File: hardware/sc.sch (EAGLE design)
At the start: 102 parts, among them K1 RT424F124, K2 RT424F124, Q1 si2305cd, Q2 8MHz, Q3 si2305cd, Q4 si2305cd, Q5 si2305cd, Q7 si2305cd, T1 BC846, T2 BC846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

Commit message: calculate resistor dividers and XT1, XT2 load caps
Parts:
- C13: value 10p -> 10pF
- C14: value 100n -> 100nF
- C18, C19: value 100nF -> 10nF
- C21, C22: value 22p -> 33pF
- C23, C24: value 22p -> 22pF
- C4: value 470pF -> 1uF
- LED2: value green -> orange
- Q2: value 8MHz -> 8MHz 18pF
- R15: value NA -> 56k
- R22, R25: value 100k -> 2M
- R24, R26: value 100k -> 240k
- Y1: value 32768Hz -> 32768Hz CFPX-217 12.5pF
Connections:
- net VBAT_IN renamed PV+
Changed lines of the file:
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@@
 <part name="GND4" library="SparkFun" deviceset="GND" device=""/>
 <part name="GND5" library="SparkFun" deviceset="GND" device=""/>
-<part name="C4" library="rcl" deviceset="C-EU" device="C0805" value="470pF"/>
+<part name="C4" library="rcl" deviceset="C-EU" device="C0805" value="1uF"/>
 <part name="GND6" library="SparkFun" deviceset="GND" device=""/>
 <part name="C6" library="rcl" deviceset="C-EU" device="C0805" value="100nF"/>
@@
 <part name="R7" library="rcl" deviceset="R-EU_" device="R0805W" value="4.7k"/>
 <part name="GND26" library="SparkFun" deviceset="GND" device=""/>
-<part name="Q2" library="Omat_komponentit" deviceset="CRYTAL" device="" value="8MHz"/>
-<part name="C21" library="rcl" deviceset="C-EU" device="C0805" value="22p"/>
-<part name="C22" library="rcl" deviceset="C-EU" device="C0805" value="22p"/>
-<part name="Y1" library="Simplex-FreqCtrl" deviceset="CRYSTAL" device="3.2X1.5" value="32768Hz"/>
-<part name="C23" library="rcl" deviceset="C-EU" device="C0805" value="22p"/>
-<part name="C24" library="rcl" deviceset="C-EU" device="C0805" value="22p"/>
+<part name="Q2" library="Omat_komponentit" deviceset="CRYTAL" device="" value="8MHz 18pF"/>
+<part name="C21" library="rcl" deviceset="C-EU" device="C0805" value="33pF"/>
+<part name="C22" library="rcl" deviceset="C-EU" device="C0805" value="33pF"/>
+<part name="Y1" library="Simplex-FreqCtrl" deviceset="CRYSTAL" device="3.2X1.5" value="32768Hz CFPX-217 12.5pF"/>
+<part name="C23" library="rcl" deviceset="C-EU" device="C0805" value="22pF"/>
+<part name="C24" library="rcl" deviceset="C-EU" device="C0805" value="22pF"/>
 <part name="GND33" library="SparkFun" deviceset="GND" device=""/>
 <part name="GND35" library="SparkFun" deviceset="GND" device=""/>
@@
 <part name="GND49" library="SparkFun" deviceset="GND" device=""/>
 <part name="R21" library="rcl" deviceset="R-EU_" device="R0805W" value="10k"/>
-<part name="R22" library="rcl" deviceset="R-EU_" device="R0805W" value="100k"/>
-<part name="R24" library="rcl" deviceset="R-EU_" device="R0805W" value="100k"/>
-<part name="R25" library="rcl" deviceset="R-EU_" device="R0805W" value="100k"/>
-<part name="R26" library="rcl" deviceset="R-EU_" device="R0805W" value="100k"/>
+<part name="R22" library="rcl" deviceset="R-EU_" device="R0805W" value="2M"/>
+<part name="R24" library="rcl" deviceset="R-EU_" device="R0805W" value="240k"/>
+<part name="R25" library="rcl" deviceset="R-EU_" device="R0805W" value="2M"/>
+<part name="R26" library="rcl" deviceset="R-EU_" device="R0805W" value="240k"/>
 <part name="GND34" library="SparkFun" deviceset="GND" device=""/>
 <part name="JP2" library="SparkFun" deviceset="M02" device="PTH" value="bat"/>
@@
 <part name="+3V2" library="supply1" deviceset="+3V3" device=""/>
 <part name="R13" library="rcl" deviceset="R-EU_" device="R0805W" value="100k"/>
-<part name="R15" library="rcl" deviceset="R-EU_" device="R0805W" value="NA"/>
+<part name="R15" library="rcl" deviceset="R-EU_" device="R0805W" value="56k"/>
 <part name="GND14" library="SparkFun" deviceset="GND" device=""/>
 <part name="C5" library="rcl" deviceset="C-EU" device="C0805" value="100nF"/>
@@
 <part name="GND20" library="SparkFun" deviceset="GND" device=""/>
 <part name="C12" library="rcl" deviceset="C-EU" device="C0805" value="10p"/>
-<part name="C13" library="rcl" deviceset="C-EU" device="C0805" value="10p"/>
+<part name="C13" library="rcl" deviceset="C-EU" device="C0805" value="10pF"/>
 <part name="GND21" library="SparkFun" deviceset="GND" device=""/>
 <part name="U$6" library="SparkFun-Connectors" deviceset="USB-MINIB" device="-5PIN"/>
@@
 <part name="R32" library="rcl" deviceset="R-EU_" device="R0805W" value="100"/>
 <part name="GND28" library="SparkFun" deviceset="GND" device=""/>
-<part name="C14" library="rcl" deviceset="C-EU" device="C0805" value="100n"/>
+<part name="C14" library="rcl" deviceset="C-EU" device="C0805" value="100nF"/>
 <part name="R33" library="rcl" deviceset="R-EU_" device="R0805W" value="33k"/>
 <part name="GND29" library="SparkFun" deviceset="GND" device=""/>
@@
 <part name="GND46" library="SparkFun" deviceset="GND" device=""/>
 <part name="U$8" library="Simplex-Switches" deviceset="TACT_SW" device="" value="USB_BSL"/>
-<part name="C18" library="rcl" deviceset="C-EU" device="C0805" value="100nF"/>
-<part name="C19" library="rcl" deviceset="C-EU" device="C0805" value="100nF"/>
+<part name="C18" library="rcl" deviceset="C-EU" device="C0805" value="10nF"/>
+<part name="C19" library="rcl" deviceset="C-EU" device="C0805" value="10nF"/>
 <part name="JP1" library="SparkFun-Connectors" deviceset="M04" device="PTH" value="i2c"/>
 <part name="SUPPLY1" library="Simplex-Power" deviceset="VCC_EN" device=""/>
@@
 <part name="SUPPLY13" library="Simplex-Power" deviceset="VCC_EN" device=""/>
 <part name="X1" library="con-phoenix-508" deviceset="MKDSN1,5/2-5,08" device=""/>
-<part name="LED2" library="led" deviceset="LED" device="CHIP-LED0805" value="green"/>
+<part name="LED2" library="led" deviceset="LED" device="CHIP-LED0805" value="orange"/>
 <part name="R27" library="rcl" deviceset="R-EU_" device="R0805W" value="1K"/>
 <part name="GND36" library="SparkFun" deviceset="GND" device=""/>
@@
 </segment>
 </net>
-<net name="VBAT_IN" class="0">
+<net name="PV+" class="0">
 <segment>
 <wire x1="71.12" y1="91.44" x2="76.2" y2="91.44" width="0.1524" layer="91"/>

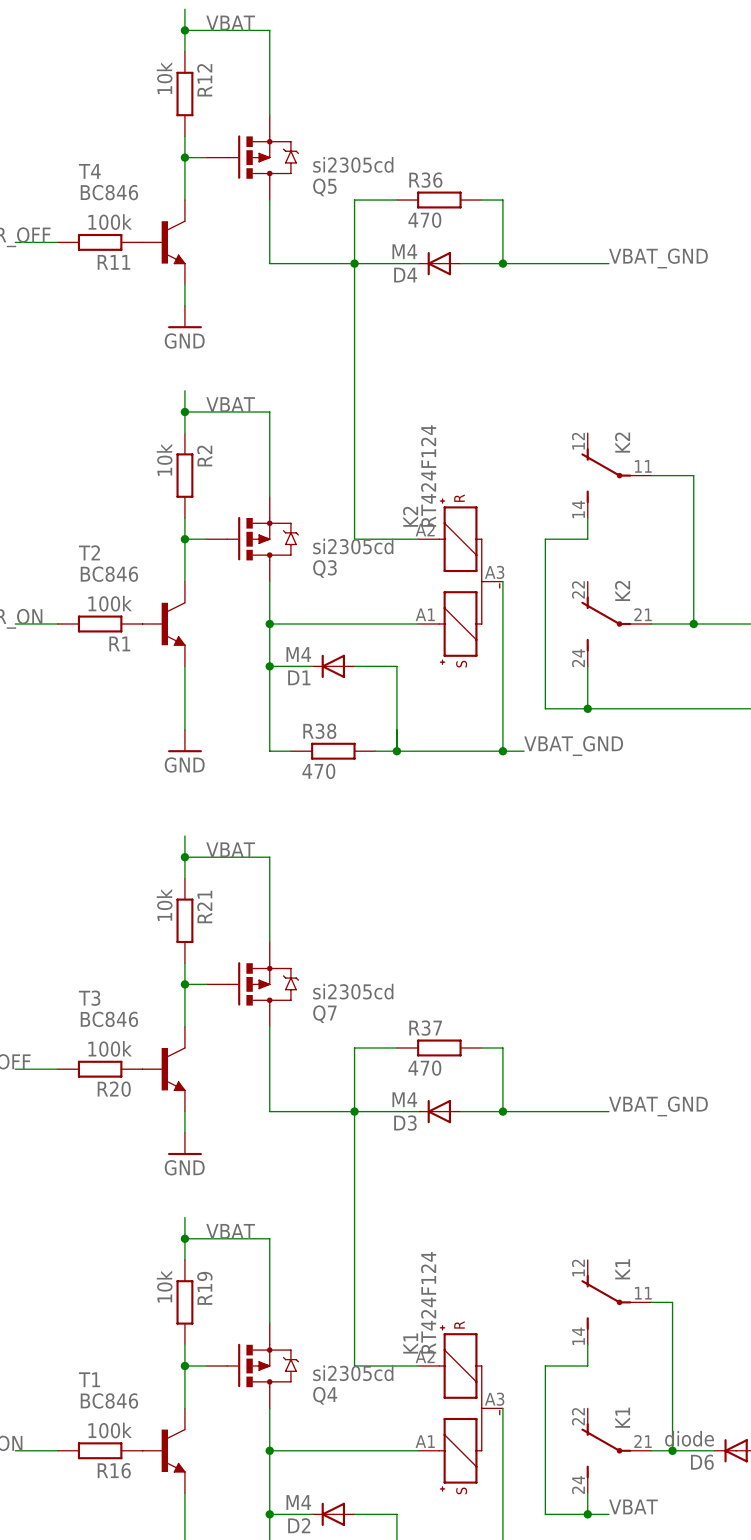
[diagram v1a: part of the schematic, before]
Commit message: use different p-mosfet
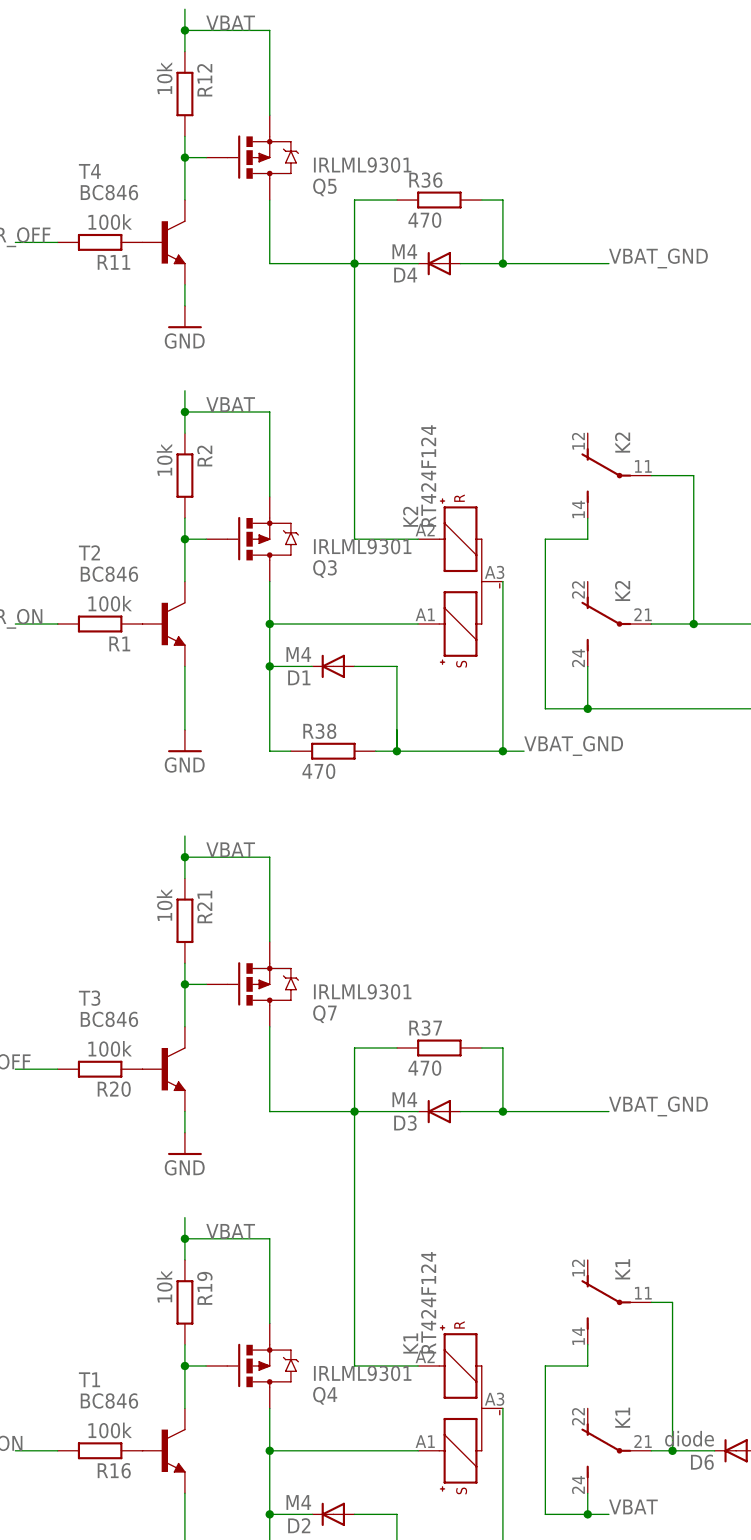
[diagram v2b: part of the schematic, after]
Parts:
- Q3, Q4, Q5, Q7: value si2305cd -> IRLML9301
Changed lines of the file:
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@@
 <part name="GND37" library="SparkFun" deviceset="GND" device=""/>
 <part name="GND47" library="SparkFun" deviceset="GND" device=""/>
-<part name="Q4" library="Simplex-DiscreteSemi" deviceset="MOSFET-PCHANNEL" device="SMD_POWER" value="si2305cd"/>
+<part name="Q4" library="Simplex-DiscreteSemi" deviceset="MOSFET-PCHANNEL" device="SMD_POWER" value="IRLML9301"/>
 <part name="T1" library="transistor" deviceset="BC846" device=""/>
 <part name="R16" library="rcl" deviceset="R-EU_" device="R0805W" value="100k"/>
 <part name="GND48" library="SparkFun" deviceset="GND" device=""/>
 <part name="R19" library="rcl" deviceset="R-EU_" device="R0805W" value="10k"/>
-<part name="Q7" library="Simplex-DiscreteSemi" deviceset="MOSFET-PCHANNEL" device="SMD_POWER" value="si2305cd"/>
+<part name="Q7" library="Simplex-DiscreteSemi" deviceset="MOSFET-PCHANNEL" device="SMD_POWER" value="IRLML9301"/>
 <part name="T3" library="transistor" deviceset="BC846" device=""/>
 <part name="R20" library="rcl" deviceset="R-EU_" device="R0805W" value="100k"/>
@@
 <part name="GND1" library="SparkFun" deviceset="GND" device=""/>
 <part name="K2" library="relay" deviceset="RT424F*" device="4" technology="12"/>
-<part name="Q3" library="Simplex-DiscreteSemi" deviceset="MOSFET-PCHANNEL" device="SMD_POWER" value="si2305cd"/>
+<part name="Q3" library="Simplex-DiscreteSemi" deviceset="MOSFET-PCHANNEL" device="SMD_POWER" value="IRLML9301"/>
 <part name="T2" library="transistor" deviceset="BC846" device=""/>
 <part name="R1" library="rcl" deviceset="R-EU_" device="R0805W" value="100k"/>
 <part name="GND7" library="SparkFun" deviceset="GND" device=""/>
 <part name="R2" library="rcl" deviceset="R-EU_" device="R0805W" value="10k"/>
-<part name="Q5" library="Simplex-DiscreteSemi" deviceset="MOSFET-PCHANNEL" device="SMD_POWER" value="si2305cd"/>
+<part name="Q5" library="Simplex-DiscreteSemi" deviceset="MOSFET-PCHANNEL" device="SMD_POWER" value="IRLML9301"/>
 <part name="T4" library="transistor" deviceset="BC846" device=""/>
 <part name="R11" library="rcl" deviceset="R-EU_" device="R0805W" value="100k"/>

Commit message: rev3
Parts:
- removed D1, D3, D4: M4, SparkFun-DiscreteSemi:DIODESMA
- removed D6: diode, diode:DIODE-C1702-05
- removed K1, K2: RT424F124, relay:RT424F124
- removed Q4, Q5, Q7: IRLML9301, Simplex-DiscreteSemi:MOSFET-PCHANNELSMD_POWER
- removed R1: 100k, rcl:R-EU_R0805W
- removed R37, R38, R39: 470, rcl:R-EU_R0805W
- removed SJ1: pwr_sel, jumper:SJ2W
- removed T2, T3, T4: BC846, transistor:BC846
- removed X1, X4: MKDSN1,5/2-5,08, con-phoenix-508:MKDSN1,5/2-5,08
- added C25, C28: 100nF, rcl:C-EUC0805
- added C26: 1uF, SparkFun-Capacitors:CAP_POLD
- added C27: 10uF, SparkFun-Capacitors:CAP_POLD
- added IC1: PB137ACV, linear:7812TV
- added IC2: INA168, burr-brown:INA168
- added LED3, LED4, LED5, LED6, LED7, LED8: green, led:LEDCHIP-LED0805
- added R17, R28: 1K, rcl:R-EU_R0805W
- added RL: 150k, rcl:R-EU_R0805W
- added RS: 0R05, Simplex-rlc:R-EU_TO220_V
- D2: value M4 -> SB560; device SparkFun-DiscreteSemi:DIODESMA -> diode:DIODE-C1702-05
- JP2: value bat -> thermistor; device SparkFun:M02PTH -> SparkFun-Connectors:M02PTH
- Q3: value IRLML9301 -> IRFR5305; device Simplex-DiscreteSemi:MOSFET-PCHANNELSMD_POWER -> transistor-power:IRFR5305
- R11: value 100k -> 30k
- R12, R21: value 10k -> 1K
- R20: value 100k -> 1K
- R36: value 470 -> 1K
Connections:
- removed net CHARGE_OFF: R20.2, U$1.19
- removed net CHARGE_ON: R16.2, U$1.18
- removed net N$31: R20.1, T3.B
- removed net N$32: Q7.G, R21.2, T3.C
- removed net N$33: K22.P, K23.P, X4-1.KL
- removed net N$35: D3.C, K11.R+, Q7.D, R37.1
- removed net N$40: SJ1.2, U$2.P$1
- removed net N$8: R1.1, T2.B
- removed net P6.2: C18.1, R22.2, R24.1, U$1.3
- removed net P6.3: C18.2, R24.2, U$1.4
- removed net R_OFF: R11.2, U$1.22
- removed net R_ON: R1.2, U$1.21
- removed net VBAT_IN_D: D6.C, K12.P, K13.P
- new net N$24: LED8.A, R36.1
- new net P1.4: R12.2, U$1.18
- new net P1.5: R17.2, U$1.19
- new net P1.7: R20.2, U$1.21
- new net P2.0: R16.2, U$1.22
- new net P5.0: C25.1, JP2.2, R11.2, U$1.5
- new net P5.1: C28.2, IC2.OUT, RL.1, U$1.6
- new net SENSE: D2.A, Q3.D, R36.2
- net GND: now also C18.2, C19.2, C25.2, C28.1, LED3.C, LED4.C, LED5.C, R24.2, R26.2; no longer JP2.1, T1.E, T2.E, T3.E, T4.E
- net N$10: now also C26.+, IC1.VI, IC2.IN-, IC2.V+, RS.1; no longer Q3.G, R2.2, T2.C
- net N$12: now also LED6.A, R21.1; no longer D1.C, K21.S+, Q3.D, R38.1
- net N$15: now also LED4.A, R17.1; no longer R11.1, T4.B
- net N$16: now also LED5.A, R20.1; no longer Q5.G, R12.2, T4.C
- net N$18: now also LED7.A, R28.1; no longer D4.C, K21.R+, Q5.D, R36.1
- net N$28: now also Q3.G, R2.2; no longer Q4.G, R19.2, T1.C
- net N$30: now also IC2.IN+, RS.2; no longer K11.S+, Q4.D, R39.1
- net N$5: now also R19.2, R2.1, T1.C; no longer K22.S, K23.S, X4-2.KL
- net N$9: now also LED3.A, R12.1; no longer JP2.2, SJ1.1
- net P6.1: now also C18.1, R22.2, R24.1; no longer C19.2, R26.2
- net PV+: now also Q3.S, R19.1, R21.2, X3-4.KL; no longer D6.A, X1-1.KL
- net SCL: now also U$1.3; no longer U$1.5
- net SDA: now also U$1.4; no longer U$1.6
- net VBAT: now also C27.+, IC1.VO, R28.2, U$2.P$1; no longer K12.S, K13.S, Q3.S, Q4.S, Q5.S, Q7.S, R12.1, R19.1, R2.1, R21.1, SJ1.3, X3-4.KL
- net VBAT_GND: now also C26.-, C27.-, IC1.GND, IC2.V-, JP2.1, LED6.C, LED7.C, LED8.C, RL.2, T1.E; no longer D1.A, D2.A, D3.A, D4.A, K11.-, K21.-, R36.2, R37.2, R38.2, R39.2, X1-2.KL
- net VCC_EN: now also R11.1
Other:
- note added: "03"
- note removed: "01"
- moved on the sheet: C1, C10, C11, C12, C13, C14, C15, C16, C17, C18, C19, C2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

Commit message: review part values
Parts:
- C18, C19: value 10nF -> 100nF
- R21, R28, R36: value 1K -> 220k
- R26: value 240k -> 470k
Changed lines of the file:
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@@
 <part name="R24" library="rcl" deviceset="R-EU_" device="R0805W" value="240k"/>
 <part name="R25" library="rcl" deviceset="R-EU_" device="R0805W" value="2M"/>
-<part name="R26" library="rcl" deviceset="R-EU_" device="R0805W" value="240k"/>
+<part name="R26" library="rcl" deviceset="R-EU_" device="R0805W" value="470k"/>
 <part name="GND34" library="SparkFun" deviceset="GND" device=""/>
 <part name="R3" library="rcl" deviceset="R-EU_" device="R0805W" value="100k"/>
@@
 <part name="GND46" library="SparkFun" deviceset="GND" device=""/>
 <part name="U$8" library="Simplex-Switches" deviceset="TACT_SW" device="" value="USB_BSL"/>
-<part name="C18" library="rcl" deviceset="C-EU" device="C0805" value="10nF"/>
-<part name="C19" library="rcl" deviceset="C-EU" device="C0805" value="10nF"/>
+<part name="C18" library="rcl" deviceset="C-EU" device="C0805" value="100nF"/>
+<part name="C19" library="rcl" deviceset="C-EU" device="C0805" value="100nF"/>
 <part name="JP1" library="SparkFun-Connectors" deviceset="M04" device="PTH" value="i2c"/>
 <part name="SUPPLY1" library="Simplex-Power" deviceset="VCC_EN" device=""/>
@@
 <part name="LED5" library="led" deviceset="LED" device="CHIP-LED0805" value="green"/>
 <part name="GND48" library="SparkFun" deviceset="GND" device=""/>
-<part name="R21" library="rcl" deviceset="R-EU_" device="R0805W" value="1K"/>
+<part name="R21" library="rcl" deviceset="R-EU_" device="R0805W" value="220k"/>
 <part name="LED6" library="led" deviceset="LED" device="CHIP-LED0805" value="green"/>
-<part name="R28" library="rcl" deviceset="R-EU_" device="R0805W" value="1K"/>
+<part name="R28" library="rcl" deviceset="R-EU_" device="R0805W" value="220k"/>
 <part name="LED7" library="led" deviceset="LED" device="CHIP-LED0805" value="green"/>
-<part name="R36" library="rcl" deviceset="R-EU_" device="R0805W" value="1K"/>
+<part name="R36" library="rcl" deviceset="R-EU_" device="R0805W" value="220k"/>
 <part name="LED8" library="led" deviceset="LED" device="CHIP-LED0805" value="green"/>
 <part name="D2" library="diode" deviceset="DIODE-" device="C1702-05" value="SB560"/>

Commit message: resistor tweaks
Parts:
- R10: value 1K -> 2k2
- R24: value 240k -> 220k
- R26: value 470k -> 330k
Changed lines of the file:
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@@
 <part name="R19" library="rcl" deviceset="R-EU_" device="R0805W" value="10k"/>
 <part name="R22" library="rcl" deviceset="R-EU_" device="R0805W" value="2M"/>
-<part name="R24" library="rcl" deviceset="R-EU_" device="R0805W" value="240k"/>
+<part name="R24" library="rcl" deviceset="R-EU_" device="R0805W" value="220k"/>
 <part name="R25" library="rcl" deviceset="R-EU_" device="R0805W" value="2M"/>
-<part name="R26" library="rcl" deviceset="R-EU_" device="R0805W" value="470k"/>
+<part name="R26" library="rcl" deviceset="R-EU_" device="R0805W" value="330k"/>
 <part name="GND34" library="SparkFun" deviceset="GND" device=""/>
 <part name="R3" library="rcl" deviceset="R-EU_" device="R0805W" value="100k"/>
@@
 <part name="R8" library="rcl" deviceset="R-EU_" device="R0805W" value="10k"/>
 <part name="LED1" library="led" deviceset="LED" device="CHIP-LED0805" value="green"/>
-<part name="R10" library="rcl" deviceset="R-EU_" device="R0805W" value="1K"/>
+<part name="R10" library="rcl" deviceset="R-EU_" device="R0805W" value="2k2"/>
 <part name="GND1" library="SparkFun" deviceset="GND" device=""/>
 <part name="U$5" library="Simplex-ICs" deviceset="TPS3613" device=""/>

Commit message: resistor value tweaks
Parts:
- RL: value 150k -> 110k
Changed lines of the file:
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@@
 <part name="LED8" library="led" deviceset="LED" device="CHIP-LED0805" value="green"/>
 <part name="D2" library="diode" deviceset="DIODE-" device="C1702-05" value="SB560"/>
-<part name="RL" library="rcl" deviceset="R-EU_" device="R0805W" value="150k"/>
+<part name="RL" library="rcl" deviceset="R-EU_" device="R0805W" value="110k"/>
 <part name="C28" library="rcl" deviceset="C-EU" device="C0805" value="100nF"/>
 <part name="GND49" library="SparkFun" deviceset="GND" device=""/>

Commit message: lower LED power
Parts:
- R12, R17, R20, R27: value 1K -> 2k2
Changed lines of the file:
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@@
 <part name="SUPPLY13" library="Simplex-Power" deviceset="VCC_EN" device=""/>
 <part name="LED2" library="led" deviceset="LED" device="CHIP-LED0805" value="orange"/>
-<part name="R27" library="rcl" deviceset="R-EU_" device="R0805W" value="1K"/>
+<part name="R27" library="rcl" deviceset="R-EU_" device="R0805W" value="2k2"/>
 <part name="GND36" library="SparkFun" deviceset="GND" device=""/>
 <part name="U$2" library="Simplex-Fuses" deviceset="RESETTABLE" device=""/>
@@
 <part name="C27" library="SparkFun-Capacitors" deviceset="CAP_POL" device="D" value="10uF"/>
 <part name="C26" library="SparkFun-Capacitors" deviceset="CAP_POL" device="D" value="1uF"/>
-<part name="R12" library="rcl" deviceset="R-EU_" device="R0805W" value="1K"/>
+<part name="R12" library="rcl" deviceset="R-EU_" device="R0805W" value="2k2"/>
 <part name="LED3" library="led" deviceset="LED" device="CHIP-LED0805" value="green"/>
 <part name="GND7" library="SparkFun" deviceset="GND" device=""/>
-<part name="R17" library="rcl" deviceset="R-EU_" device="R0805W" value="1K"/>
+<part name="R17" library="rcl" deviceset="R-EU_" device="R0805W" value="2k2"/>
 <part name="LED4" library="led" deviceset="LED" device="CHIP-LED0805" value="green"/>
 <part name="GND43" library="SparkFun" deviceset="GND" device=""/>
-<part name="R20" library="rcl" deviceset="R-EU_" device="R0805W" value="1K"/>
+<part name="R20" library="rcl" deviceset="R-EU_" device="R0805W" value="2k2"/>
 <part name="LED5" library="led" deviceset="LED" device="CHIP-LED0805" value="green"/>
 <part name="GND48" library="SparkFun" deviceset="GND" device=""/>
